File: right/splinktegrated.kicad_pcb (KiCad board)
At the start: 4 copper layers, 72.5 x 88.4 mm, 81 parts, among them J1 USB_C_Receptacle_USB2.0, J10 NA_Ribbon, J13 Conn_01x01_Socket, J14 Cirque, J15 Conn_01x01_Socket, J16 Conn_01x01_Socket, J17 Conn_01x01_Socket, J18 USB_C_Receptacle_USB2.0, J19 Conn_01x01_Socket, J20 Conn_01x01_Socket, J5 Conn_01x02, J6 Cirque, J7 NA_trackball, J8 NA_Ribbon, J9 NA_RGB, Q4 AO3401A, Q5 AO3401A, SW2 NA_SW_SPST, U1 RP2040, U2 USBLC6-2P6, U3 XC6210B332MR-G, U4 USBLC6-2P6, U5 W25Q128JVS, U6 74LVC1T45, Y1 Crystal_GND24

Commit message: routing
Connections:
- J6 pad 10: SCL -> SDA
- J6 pad 9: SDA -> SCL
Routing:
- net SDA: track 43.0 -> 44.3 mm
- net GND: track 52.4 -> 53.2 mm
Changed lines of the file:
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@@
 			(size 0.28 1.25)
 			(layers "F.Cu" "F.Mask" "F.Paste")
-			(net 53 "SDA")
+			(net 54 "SCL")
 			(pinfunction "Pin_9")
 			(pintype "passive")
@@
 			(size 0.28 1.25)
 			(layers "F.Cu" "F.Mask" "F.Paste")
-			(net 54 "SCL")
+			(net 53 "SDA")
 			(pinfunction "Pin_10")
 			(pintype "passive")
@@
 	)
 	(segment
+		(start 151.01 129.59)
+		(end 151.01 130.8)
+		(width 0.3)
+		(layer "F.Cu")
+		(net 2)
+	)
+	(segment
 		(start 159.6 88.9)
 		(end 159.35 88.65)
@@
 	)
 	(segment
-		(start 151.01 129.59)
-		(end 151.3 129.3)
-		(width 0.3)
-		(layer "F.Cu")
-		(net 2)
-	)
-	(segment
 		(start 157.96 104.1)
 		(end 158.7 104.1)
@@
 	)
 	(segment
-		(start 151.01 130.8)
+		(start 151.616897 128.983103)
 		(end 151.01 129.59)
 		(width 0.3)
@@
 	)
 	(segment
+		(start 151.984518 128.983103)
+		(end 151.616897 128.983103)
+		(width 0.3)
+		(layer "F.Cu")
+		(net 2)
+	)
+	(segment
 		(start 162.05 99.58)
 		(end 161.9 99.43)
@@
 	)
 	(via
-		(at 151.3 129.3)
+		(at 151.984518 128.983103)
 		(size 0.6)
 		(drill 0.3)
@@
 	)
 	(segment
-		(start 149.8 129.25)
-		(end 149.8 129.6)
+		(start 150.774228 129.025772)
+		(end 150.631 129.169)
 		(width 0.11)
 		(layer "F.Cu")
@@
 	)
 	(segment
-		(start 149.8 129.6)
-		(end 150.01 129.81)
+		(start 150.631 129.169)
+		(end 150.631 130.679)
 		(width 0.11)
 		(layer "F.Cu")
@@
 	)
 	(segment
-		(start 150.01 129.81)
-		(end 150.01 130.8)
+		(start 150.631 130.679)
+		(end 150.51 130.8)
 		(width 0.11)
 		(layer "F.Cu")
@@
 	)
 	(via
-		(at 150.4 97)
+		(at 150.774228 129.025772)
 		(size 0.45)
 		(drill 0.2)
@@
 	)
 	(via
-		(at 149.8 129.25)
+		(at 150.4 97)
 		(size 0.45)
 		(drill 0.2)
@@
 	)
 	(segment
+		(start 149.8 129.25)
+		(end 150.55 129.25)
+		(width 0.11)
+		(layer "B.Cu")
+		(net 53)
+	)
+	(segment
+		(start 150.55 129.25)
+		(end 150.774228 129.025772)
+		(width 0.11)
+		(layer "B.Cu")
+		(net 53)
+	)
+	(segment
 		(start 148.4 103.6)
 		(end 149.3 102.7)
@@
 	)
 	(segment
-		(start 150.51 130.8)
-		(end 150.51 129.025772)
+		(start 150.01 130.8)
+		(end 150.01 128.908458)
 		(width 0.11)
 		(layer "F.Cu")
@@
 	)
 	(segment
-		(start 150.51 129.025772)
-		(end 150.41 128.925772)
+		(start 150.01 128.908458)
+		(end 149.886542 128.785)
 		(width 0.11)
 		(layer "F.Cu")
@@
 	)
 	(via
-		(at 150.41 128.925772)
+		(at 149.886542 128.785)
 		(size 0.45)
 		(drill 0.2)
@@
 	)
 	(segment
-		(start 145.121 115.991541)
-		(end 146.621 114.491542)
+		(start 148.491541 103.821)
+		(end 149.521 102.791542)
 		(width 0.11)
 		(layer "B.Cu")
@@
 	)
 	(segment
-		(start 147.562542 128.45)
-		(end 145.121 126.008458)
+		(start 145.121 115.991541)
+		(end 146.621 114.491542)
 		(width 0.11)
 		(layer "B.Cu")
@@
 	)
 	(segment
-		(start 146.991542 103.821)
-		(end 148.491541 103.821)
+		(start 150.7 97.4)
+		(end 151.1 97)
 		(width 0.11)
 		(layer "B.Cu")
@@
 	)
 	(segment
-		(start 145.121 126.008458)
-		(end 145.121 115.991541)
+		(start 150.7 99.612542)
+		(end 150.7 97.4)
 		(width 0.11)
 		(layer "B.Cu")
@@
 	)
 	(segment
-		(start 150.7 99.612542)
-		(end 150.7 97.4)
+		(start 146.621 104.191542)
+		(end 146.991542 103.821)
 		(width 0.11)
 		(layer "B.Cu")
@@
 	)
 	(segment
-		(start 148.491541 103.821)
-		(end 149.521 102.791542)
+		(start 145.121 126.008458)
+		(end 145.121 115.991541)
 		(width 0.11)
 		(layer "B.Cu")
@@
 	)
 	(segment
-		(start 146.621 104.191542)
-		(end 146.991542 103.821)
+		(start 146.991542 103.821)
+		(end 148.491541 103.821)
 		(width 0.11)
 		(layer "B.Cu")
@@
 	)
 	(segment
-		(start 149.934228 128.45)
+		(start 149.551542 128.45)
 		(end 147.562542 128.45)
 		(width 0.11)
@@
 	)
 	(segment
-		(start 149.521 102.791542)
-		(end 149.521 100.791542)
+		(start 149.521 100.791542)
+		(end 150.7 99.612542)
 		(width 0.11)
 		(layer "B.Cu")
@@
 	)
 	(segment
-		(start 150.41 128.925772)
-		(end 149.934228 128.45)
+		(start 149.521 102.791542)
+		(end 149.521 100.791542)
 		(width 0.11)
 		(layer "B.Cu")
@@
 	)
 	(segment
-		(start 149.521 100.791542)
-		(end 150.7 99.612542)
+		(start 146.621 114.491542)
+		(end 146.621 104.191542)
 		(width 0.11)
 		(layer "B.Cu")
@@
 	)
 	(segment
-		(start 146.621 114.491542)
-		(end 146.621 104.191542)
+		(start 147.562542 128.45)
+		(end 145.121 126.008458)
 		(width 0.11)
 		(layer "B.Cu")
@@
 	)
 	(segment
-		(start 150.7 97.4)
-		(end 151.1 97)
+		(start 149.886542 128.785)
+		(end 149.551542 128.45)
 		(width 0.11)
 		(layer "B.Cu")
@@
 	)
 	(segment
-		(start 150.75 128.7)
-		(end 149.690948 127.640948)
+		(start 148.909052 127.640948)
+		(end 148.568105 127.3)
 		(width 0.11)
 		(layer "B.Cu")
@@
 	)
 	(segment
-		(start 148.568105 127.3)
-		(end 147.5 127.3)
+		(start 157.75 132)
+		(end 156.45 133.3)
 		(width 0.11)
 		(layer "B.Cu")
@@
 	)
 	(segment
-		(start 155.416458 107.983542)
-		(end 155.416458 106.671)
+		(start 149.940948 127.640948)
+		(end 148.909052 127.640948)
 		(width 0.11)
 		(layer "B.Cu")
@@
 	)
 	(segment
-		(start 148.909052 127.640948)
-		(end 148.568105 127.3)
+		(start 154.568105 133.3)
+		(end 152.234052 130.965948)
 		(width 0.11)
 		(layer "B.Cu")
@@
 	)
 	(segment
-		(start 154.836362 109.663638)
-		(end 156.1 108.4)
+		(start 155.416458 107.983542)
+		(end 155.416458 106.671)
 		(width 0.11)
 		(layer "B.Cu")
@@
 	)
 	(segment
-		(start 159 110.8)
-		(end 158.687458 110.8)
+		(start 152.234052 129.934052)
+		(end 149.940948 127.640948)
 		(width 0.11)
 		(layer "B.Cu")
@@
 	)
 	(segment
-		(start 155.149541 103.429)
-		(end 154.779 103.429)
+		(start 154.836362 109.663638)
+		(end 156.1 108.4)
 		(width 0.11)
 		(layer "B.Cu")
@@
 	)
 	(segment
-		(start 154.836362 110.488579)
-		(end 154.836362 109.663638)
+		(start 159 110.8)
+		(end 158.687458 110.8)
 		(width 0.11)
 		(layer "B.Cu")
@@
 	)
 	(segment
-		(start 157.75 132)
-		(end 156.45 133.3)
+		(start 155.149541 103.429)
+		(end 154.779 103.429)
 		(width 0.11)
 		(layer "B.Cu")
@@
 	)
 	(segment
-		(start 149.690948 127.640948)
-		(end 148.909052 127.640948)
+		(start 154.836362 110.488579)
+		(end 154.836362 109.663638)
 		(width 0.11)
 		(layer "B.Cu")
@@
 	)
 	(segment
-		(start 156.45 133.3)
-		(end 154.568105 133.3)
+		(start 148.568105 127.3)
+		(end 147.5 127.3)
 		(width 0.11)
 		(layer "B.Cu")
@@
 	)
 	(segment
-		(start 150.8 128.7)
-		(end 150.75 128.7)
+		(start 156.097783 111.75)
+		(end 154.836362 110.488579)
 		(width 0.11)
 		(layer "B.Cu")
@@
 	)
 	(segment
-		(start 156.097783 111.75)
-		(end 154.836362 110.488579)
+		(start 156.45 133.3)
+		(end 154.568105 133.3)
 		(width 0.11)
 		(layer "B.Cu")
@@
 	)
 	(segment
-		(start 154.568105 133.3)
-		(end 150.8 129.531896)
+		(start 152.234052 130.965948)
+		(end 152.234052 129.934052)
 		(width 0.11)
 		(layer "B.Cu")
@@
 		(width 0.11)
 		(layer "B.Cu")
-		(net 58)
-	)
-	(segment
-		(start 150.8 129.531896)
-		(end 150.8 128.7)
-		(width 0.11)
-		(layer "B.Cu")

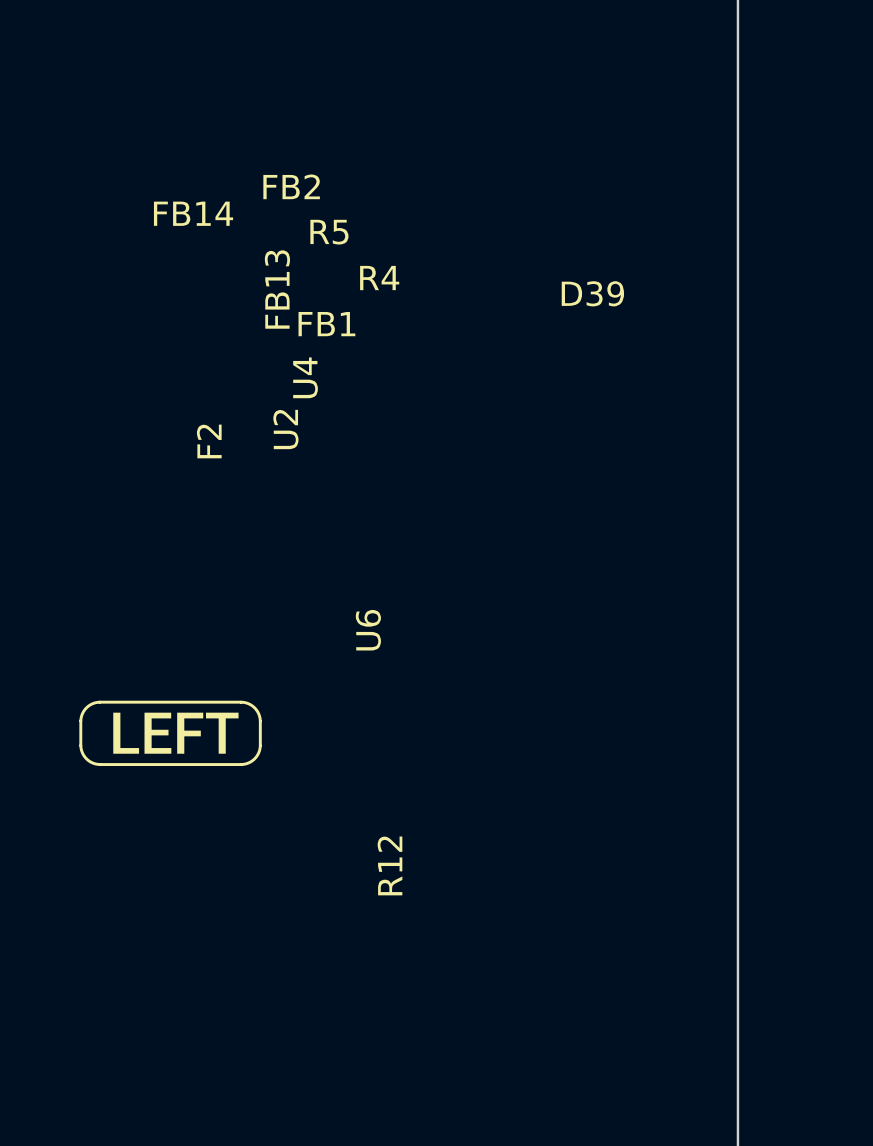
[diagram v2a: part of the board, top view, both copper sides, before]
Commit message: start renaming right side labels for later incorporation
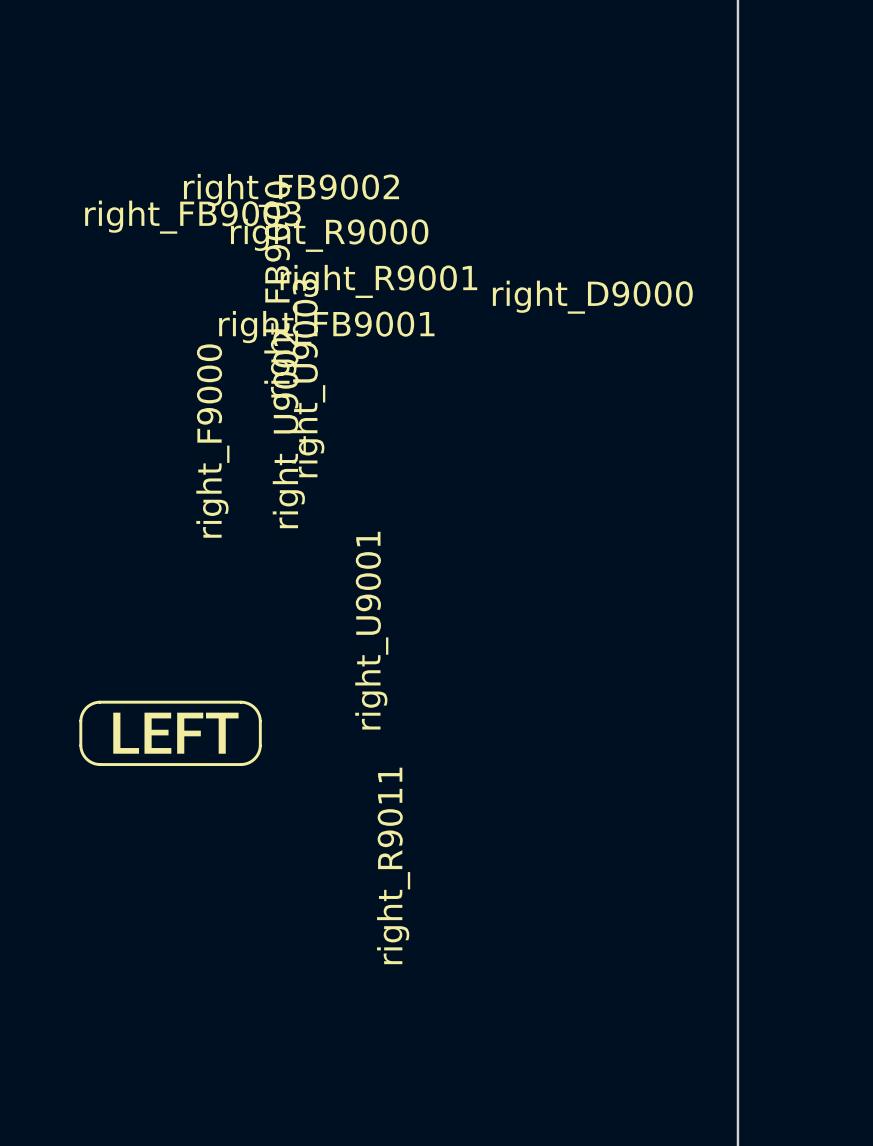
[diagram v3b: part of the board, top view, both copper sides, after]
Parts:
- renumbered NA_JP6 to NA_JP1, SW2 to SW1, kibuzzard-61F01B61 to kibuzzard-1, C1 to right_C9000, C8 to right_C9001, C9 to right_C9002, C11 to right_C9003, C12 to right_C9004, C13 to right_C9005, C14 to right_C9006, C10 to right_C9007, C2 to right_C9008, C3 to right_C9009, C4 to right_C9010, C5 to right_C9011, C6 to right_C9012, C7 to right_C9013, D39 to right_D9000, D2 to right_D9001, D1 to right_D9002, F2 to right_F9000, F1 to right_F9001, FB13 to right_FB9000, FB1 to right_FB9001, FB2 to right_FB9002, FB14 to right_FB9003, H5008 to right_H9000, H2 to right_H9001, H5008 to right_H9002, H1 to right_H9003, H5008 to right_H9004, H5008 to right_H9005, H5008 to right_H9006, H5008 to right_H9007, H5008 to right_H9008, H5008 to right_H9009, J18 to right_J9000, J1 to right_J9001, J20 to right_J9002, J19 to right_J9003, J5 to right_J9004, J8 to right_J9005, J9 to right_J9006, J10 to right_J9007, J7 to right_J9008, J15 to right_J9009, J14 to right_J9010, J17 to right_J9011, J16 to right_J9012, J13 to right_J9013, J6 to right_J9014, NA_JP5 to right_NA_JP9000, NA_JP7 to right_NA_JP9001, Q5 to right_Q9000, Q4 to right_Q9001, R5 to right_R9000, R4 to right_R9001, R1 to right_R9002, R2 to right_R9003, R3 to right_R9004, R6 to right_R9005, R7 to right_R9006, R8 to right_R9007, R9 to right_R9008, R10 to right_R9009, R11 to right_R9010, R12 to right_R9011, U3 to right_U9000, U6 to right_U9001, U2 to right_U9002, U4 to right_U9003, U5 to right_U9004, U1 to right_U9005, Y1 to right_Y9000, kibuzzard-6208EFFE to right_kibuzzard-9000, kibuzzard-61F01B61 to right_kibuzzard-9001

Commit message: start renaming nets
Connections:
- net +3V3 renamed right_+3V3
- net /D+ renamed /D+_daughter
- net /D- renamed /D-_daughter
- net /QSPI_D0 renamed /right_QSPI_D0
- net /QSPI_D1 renamed /right_QSPI_D1
- net /QSPI_D2 renamed /right_QSPI_D2
- net /QSPI_D3 renamed /right_QSPI_D3
- net /QSPI_SCLK renamed /right_QSPI_SCLK
- net /QSPI_~{CS} renamed /right_QSPI_~{CS}
- net VBUS renamed right_VBUS
- net V_USB_DETECT renamed right_V_USB_DETECT
- net serial_l renamed right_serial_l
- net serial_l2 renamed right_serial_l2
- NA_JP1 pad 2: GND -> right_GND
- right_C9000 pad 2: GND -> right_GND
- right_C9001 pad 2: GND -> right_GND
- right_C9002 pad 2: GND -> right_GND
- right_C9003 pad 2: GND -> right_GND
- right_C9004 pad 2: GND -> right_GND
- right_C9005 pad 2: GND -> right_GND
- right_C9006 pad 2: GND -> right_GND
- right_C9007 pad 2: GND -> right_GND
- right_C9008 pad 2: GND -> right_GND
- right_C9009 pad 2: GND -> right_GND
- right_C9010 pad 2: GND -> right_GND
- right_C9011 pad 2: GND -> right_GND
- right_C9012 pad 2: GND -> right_GND
- right_C9013 pad 2: GND -> right_GND
- right_D9000 pad 2: GND -> right_GND
- right_FB9001 pad 1: GND -> right_GND
- right_FB9002 pad 1: GND -> right_GND
- right_H9001 pad 1: GND -> right_GND
- right_H9003 pad 1: GND -> right_GND
- right_J9000 pad A1: GND -> right_GND
- right_J9000 pad A12: GND -> right_GND
- right_J9000 pad B1: GND -> right_GND
- right_J9000 pad B12: GND -> right_GND
- right_J9001 pad A1: GND -> right_GND
- right_J9001 pad A12: GND -> right_GND
- right_J9001 pad B1: GND -> right_GND
- right_J9001 pad B12: GND -> right_GND
- right_J9004 pad 1: GND -> right_GND
- right_J9006 pad 2: GND -> right_GND
- right_J9008 pad 6: GND -> right_GND
- right_J9014 pad 11: GND -> right_GND
- right_Q9000 pad 1: GND -> right_GND
- right_Q9001 pad 1: GND -> right_GND
- right_R9000 pad 2: GND -> right_GND
- right_R9001 pad 2: GND -> right_GND
- right_R9002 pad 1: GND -> right_GND
- right_R9003 pad 1: /~{RESET} -> /right_~{RESET}
- right_R9010 pad 1: GND -> right_GND
- right_U9000 pad 2: GND -> right_GND
- right_U9001 pad 2: GND -> right_GND
- right_U9002 pad 2: GND -> right_GND
- right_U9003 pad 2: GND -> right_GND
- right_U9004 pad 4: GND -> right_GND
- right_U9005 pad 19: GND -> right_GND
- right_U9005 pad 26: /~{RESET} -> /right_~{RESET}
- right_U9005 pad 57: GND -> right_GND
- right_Y9000 pad 2: GND -> right_GND
- right_Y9000 pad 4: GND -> right_GND
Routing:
- net right_+3V3: track 40.1 -> 0.00 mm
- net (no net): track 0.00 -> 40.1 mm
- net right_GND: vias 0 -> 36
- net GND: vias 36 -> 0
- added copper zone on B.Cu, net right_GND
- added copper zone on F.Cu, net right_GND
- added copper zone on In1.Cu, net right_GND
- removed copper zone on B.Cu, net GND
- removed copper zone on F.Cu, net GND
- removed copper zone on In1.Cu, net GND

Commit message: nets
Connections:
- net /D10 renamed /right_D10
- net /D11 renamed /right_D11
- net /D13 renamed /right_D13
- net /D14 renamed /right_D14
- net /LED renamed /right_LED
- net /VBUS_DET renamed /right_VBUS_DET
- net /hand renamed /right_hand
- net /right_QSPI_SCLK renamed /right_QSPI_right_SCLK
- net SCL renamed right_SCL
- net SDA renamed right_SDA
- net col1_l renamed right_col1_l
- net col2_l renamed right_col2_l
- net col3_l renamed right_col3_l
- net col4_l renamed right_col4_l
- net col5_l renamed right_right_col5_l
- net col6_l renamed right_col6_l
- net miso_l renamed right_MISO_l
- net mosi_l renamed right_MOSI_l
- net rgb_3v3 renamed right_rgb_3v3
- net row1_l renamed right_row1_l
- net row2_l renamed right_row2_l
- net row3_l renamed right_row3_l
- net row4_l renamed right_row4_l
- net row5_l renamed right_row5_l
- net sc_l renamed right_sc_l
- net ss_l renamed right_ss_l
- SW1 pad 1: /~{RESET} -> /right_~{RESET}
- SW1 pad 2: GND -> right_GND
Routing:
- net right_GND: track 0.00 -> 53.2 mm
- net GND: track 53.2 -> 0.00 mm
- net /~{RESET}: track 47.6 -> 0.00 mm, vias 5 -> 0
- net /right_~{RESET}: track 0.00 -> 47.6 mm, vias 0 -> 5
- net right_+3V3: track 0.00 -> 40.1 mm
- net (no net): track 40.1 -> 0.00 mm
